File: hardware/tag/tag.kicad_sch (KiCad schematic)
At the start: 118 parts, among them J1 USB_C_Receptacle_USB2.0_16P, J2 BATTERY, J3 BLE_Conn, J4 SOURCE, J5 STM SWD, J6 I2C, J7 UART, J8 BLE SWD, J9 I2C, Q1 AO664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

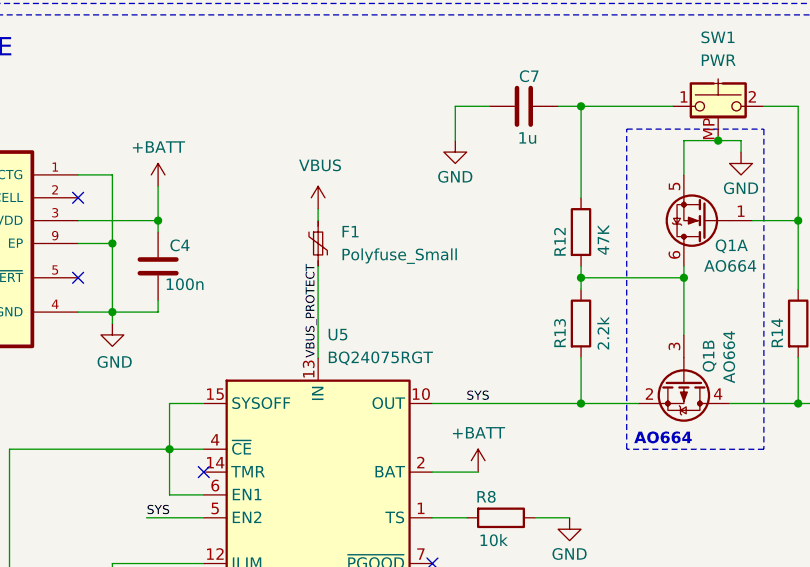
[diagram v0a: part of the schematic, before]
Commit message: Update: schematic adjustments
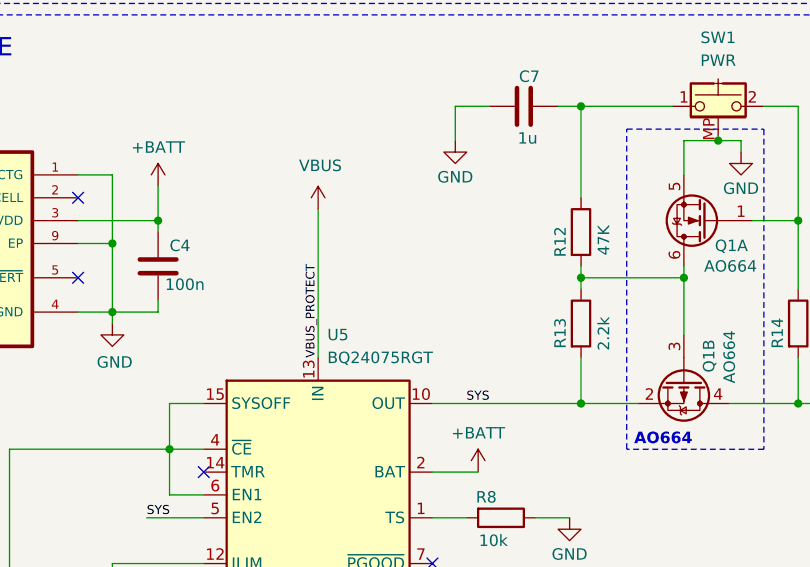
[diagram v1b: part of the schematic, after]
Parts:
- removed F1: Polyfuse_Small, Fuse:Fuse_1206_3216Metric, symbol Device:Polyfuse_Small
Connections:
- net VBUS_PROTECT is gone; now on net VBUS: C6.2, U5.13 (IN)
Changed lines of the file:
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@@
 	(wire
 		(pts
-			(xy 93.98 153.67) (xy 93.98 154.94)
-		)
-		(stroke
-			(width 0)
-			(type default)
-		)
-	)
-	(wire
-		(pts
 			(xy 179.07 222.25) (xy 179.07 237.49)
 		)
@@
 	(wire
 		(pts
+			(xy 93.98 153.67) (xy 93.98 170.18)
+		)
+		(stroke
+			(width 0)
+			(type default)
+		)
+	)
+	(wire
+		(pts
 			(xy 71.12 165.1) (xy 71.12 166.37)
 		)
@@
 	(wire
 		(pts
-			(xy 93.98 160.02) (xy 93.98 170.18)
-		)
-		(stroke
-			(width 0)
-			(type default)
-		)
-	)
-	(wire
-		(pts
 			(xy 127 212.09) (xy 127 215.9)
 		)
@@
 					(unit 1)
 				)
-			)
-		)
-	)
-	(symbol
-		(lib_id "Device:Polyfuse_Small")
-		(at 93.98 157.48 0)
-		(unit 1)
-		(exclude_from_sim no)
-		(in_bom yes)
-		(on_board yes)
-		(dnp no)
-		(property "Reference" "F1"
-			(at 96.52 156.2099 0)
-			(effects
-				(font
-					(size 1.27 1.27)
-				)
-				(justify left)
-			)
-		)
-		(property "Value" "Polyfuse_Small"
-			(at 96.52 158.7499 0)
-			(effects
-				(font
-					(size 1.27 1.27)
-				)
-				(justify left)
-			)
-		)
-		(property "Footprint" "Fuse:Fuse_1206_3216Metric"
-			(at 95.25 162.56 0)
-			(effects
-				(font
-					(size 1.27 1.27)
-				)
-				(justify left)
-				(hide yes)
-			)
-		)
-		(property "Datasheet" "~"
-			(at 93.98 157.48 0)
-			(effects
-				(font
-					(size 1.27 1.27)
-				)
-				(hide yes)
-			)
-		)
-		(property "Description" "Resettable fuse, polymeric positive temperature coefficient, small symbol"
-			(at 93.98 157.48 0)
-			(effects
-				(font
-					(size 1.27 1.27)
-				)
-				(hide yes)
-			)
-		)
-		(pin "2"
-		)
-		(pin "1"
-		)
-		(instances
-			(project "tag"
-				(path "/36ff3ade-5474-48a6-a94c-a185611a6890"
-					(reference "F1")
-					(unit 1)
-				)

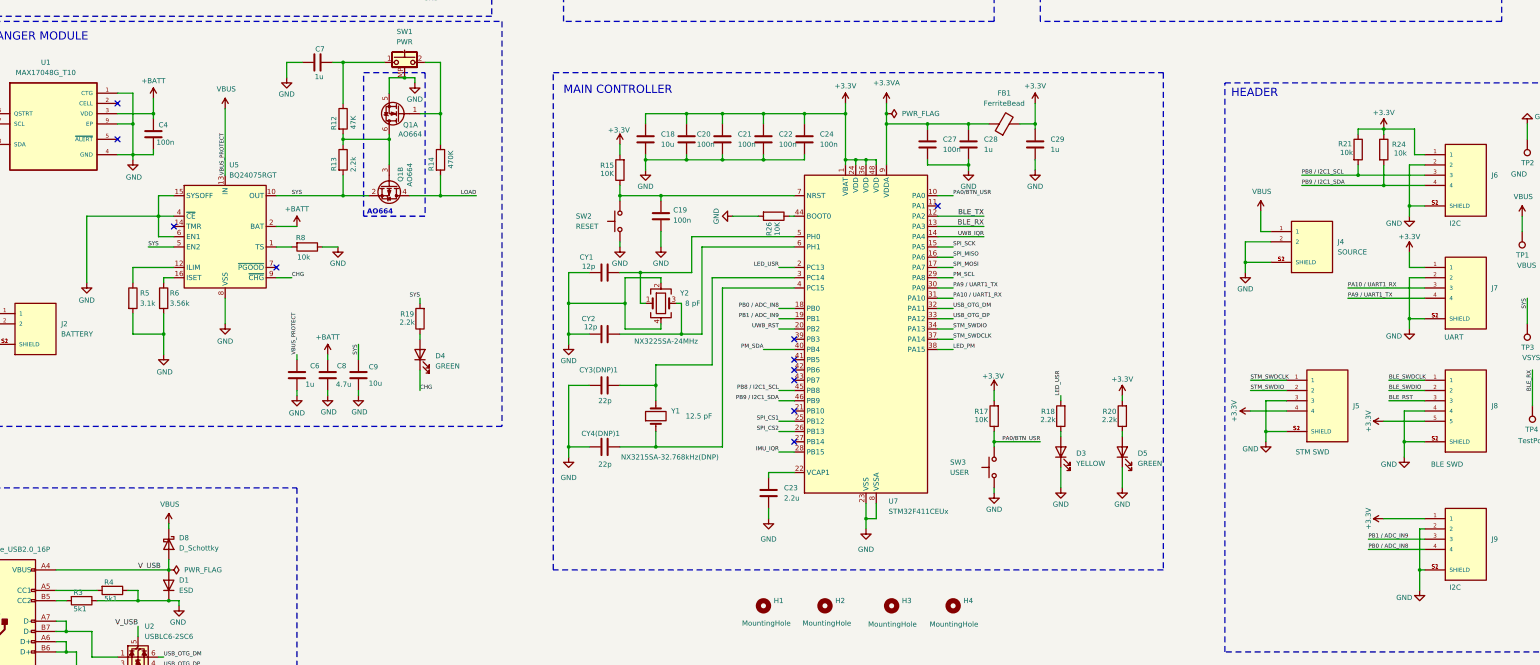
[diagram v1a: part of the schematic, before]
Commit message: Update: Change the on/off power logic on tag
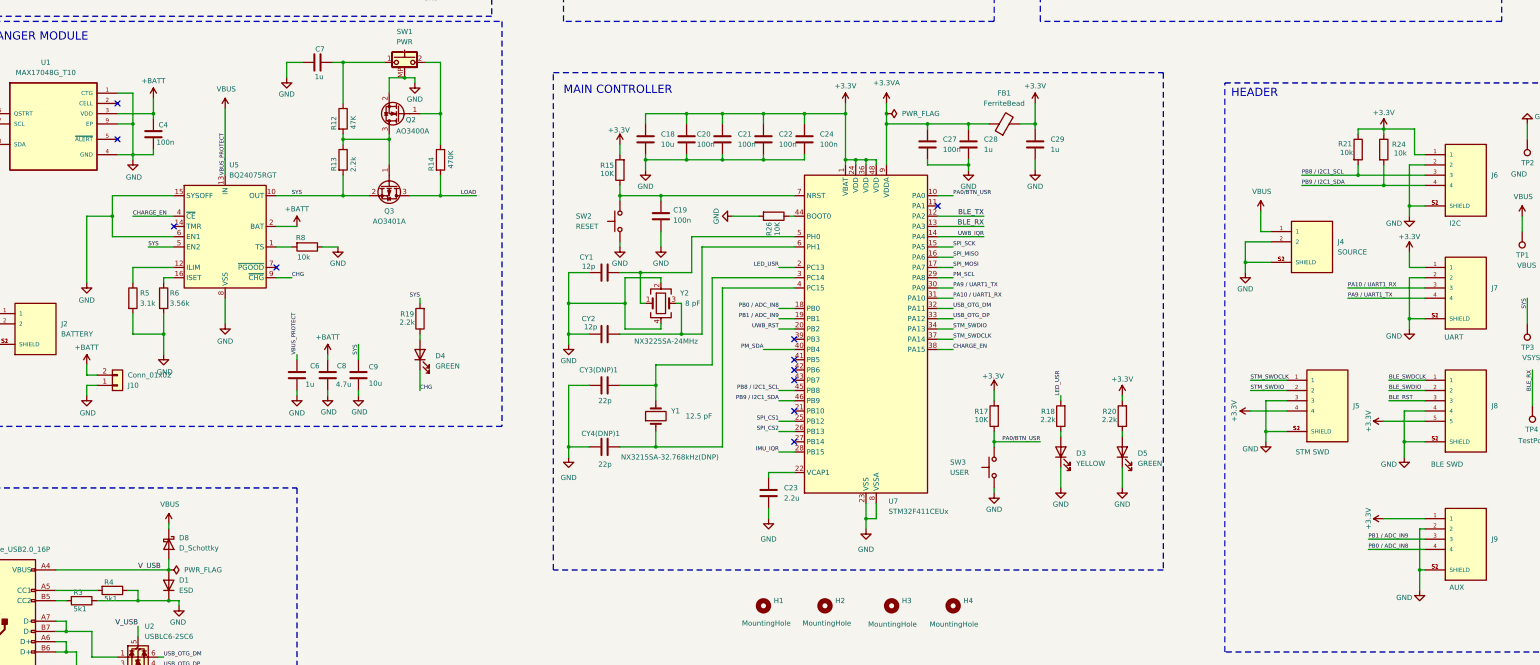
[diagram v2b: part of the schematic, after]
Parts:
- removed Q1: AO664, Package_SO:TSOP-6_1.65x3.05mm_P0.95mm, symbol Transistor_FET:IRF7309PBF
- added J10: Conn_01x02, Connector_Wire:SolderWire-0.5sqmm_1x02_P4.6mm_D0.9mm_OD2.1mm, symbol Connector_Generic:Conn_01x02
- added Q2: AO3400A, Package_TO_SOT_SMD:SOT-23, symbol Transistor_FET:AO3400A
- added Q3: AO3401A, Package_TO_SOT_SMD:SOT-23, symbol Transistor_FET:AO3401A
- C9: footprint Capacitor_SMD:C_0805_2012Metric_Pad1.18x1.45mm_HandSolder -> Capacitor_SMD:C_0805_2012Metric
- J9: value I2C -> AUX
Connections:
- net +BATT: now also J10.2 (Pin_2)
- net GND: now also J10.1 (Pin_1), Q2.2 (S); no longer U5.4 (~{CE})
- net LOAD: now also Q3.3 (D)
- net SYS: now also Q3.2 (S)
- net at R12.2, R13.1: now also Q2.3 (D), Q3.1 (G)
- net at R14.1, SW1.2: now also Q2.1 (G)
- net LED_PM renamed CHARGE_EN
- net CHARGE_EN: now also U5.4 (~{CE})
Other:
- note removed: "AO664"

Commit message: feat: Release final hardware for tag & anchor
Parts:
- C7: value 1u -> 100n
- J10: footprint Connector_Wire:SolderWire-0.5sqmm_1x02_P4.6mm_D0.9mm_OD2.1mm -> Connector_Wire:SolderWire-0.1sqmm_1x02_P3.6mm_D0.4mm_OD1mm
- Q2: value AO3400A -> AO3404A
- Q3: value AO3401A -> AO3407A
- R12: value 47K -> 100k
- R13: value 2.2k -> 10k
- R14: value 470K -> 10k
- TP10: value TestPoint -> MOSI
- TP11: value TestPoint -> TX
- TP12: value TestPoint -> RST
- TP13: value TestPoint -> MISO
- TP14: value TestPoint -> CS1
- TP15: value TestPoint -> CS2
- TP4: value TestPoint -> RX
- TP8: footprint TestPoint:TestPoint_Pad_D1.5mm -> TestPoint:TestPoint_Pad_1.0x1.0mm
- TP9: value TestPoint -> SCK
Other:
- moved on the sheet: J10, J2
